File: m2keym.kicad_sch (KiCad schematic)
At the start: 0 parts

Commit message: [#56643] Create buses for interfaces, assign buses to blocks
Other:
- company: (none) -> Antmicro Ltd.
- title: (none) -> Com Express 7 baseboard
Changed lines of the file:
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@@
 (kicad_sch (version 20230121) (generator eeschema)
-  (paper "A4")
+  (paper "A3")
+  (title_block
+    (title "Com Express 7 baseboard")
+    (date "2024-03-22")
+    (rev "1.0.0")
+    (company "Antmicro Ltd.")
+  )
   (hierarchical_label "PCIe_x4{PCIe}" (shape input) (at 66.04 63.5 180) (fields_autoplaced)
     (effects (font (size 1.27 1.27)) (justify right))

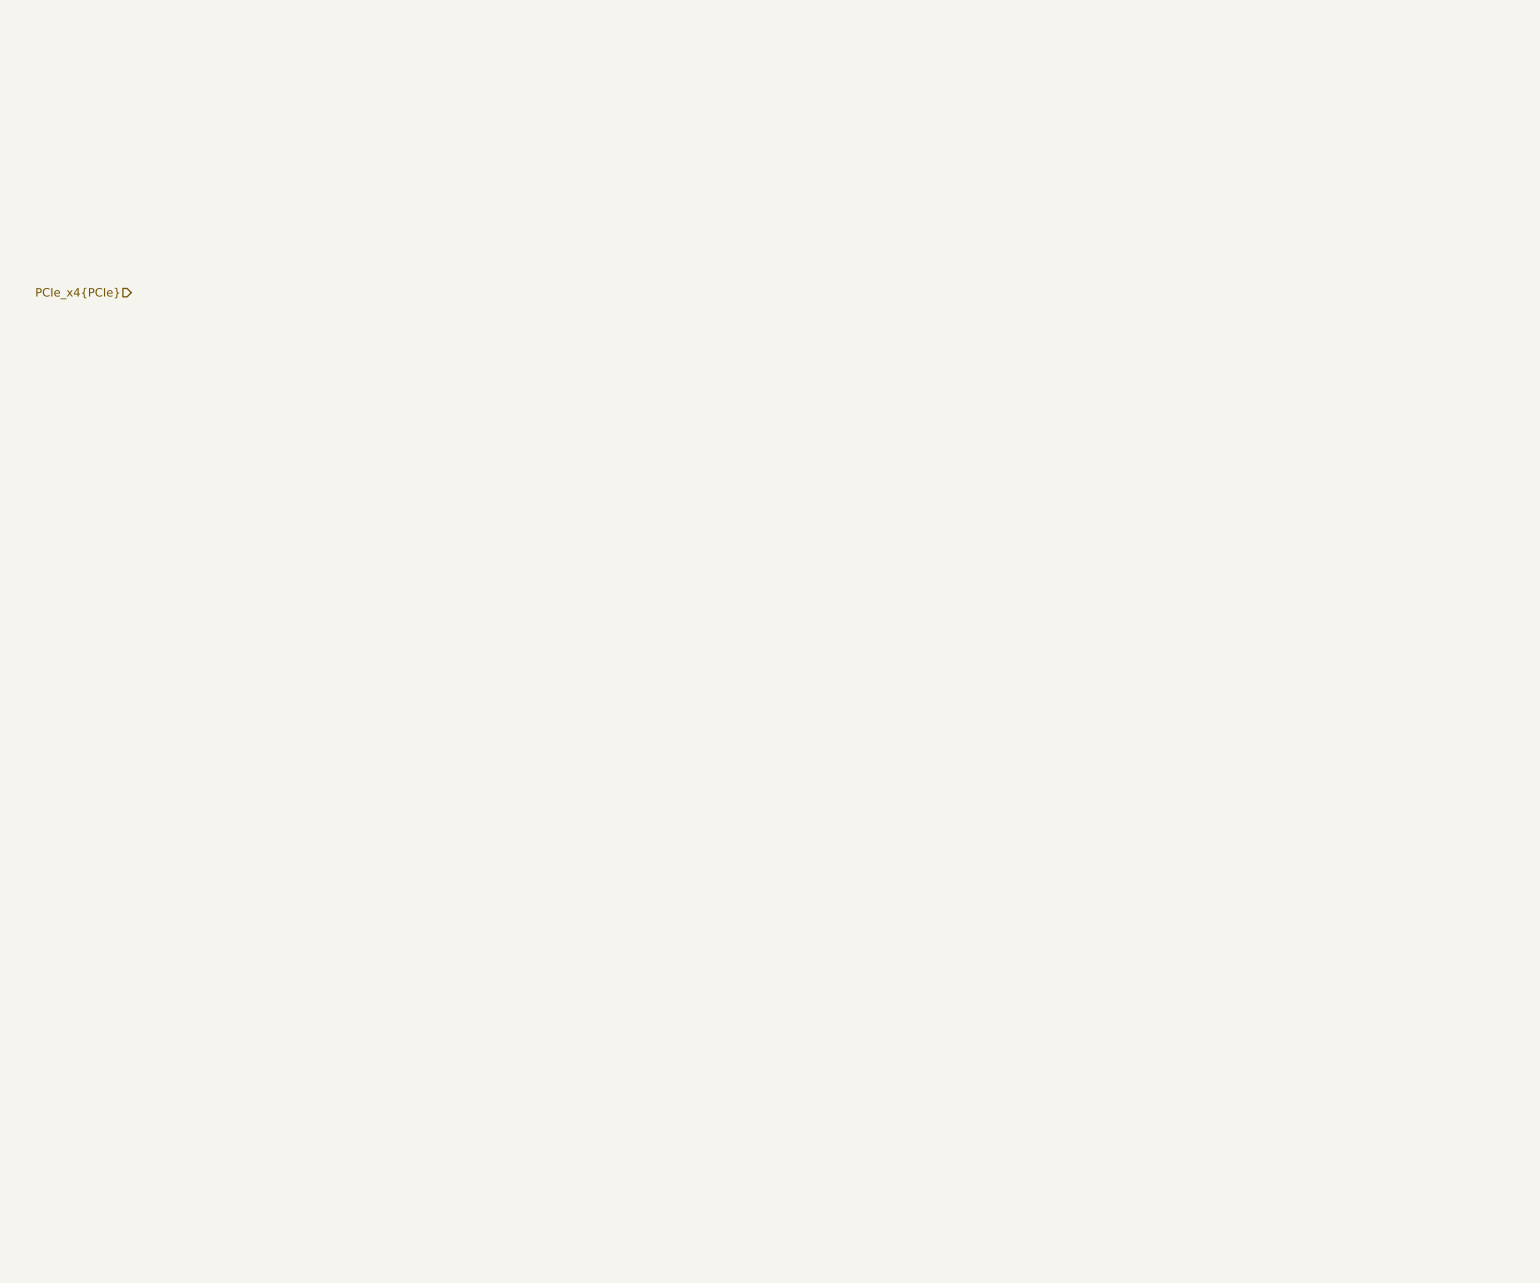
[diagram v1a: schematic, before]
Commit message: [#57056] Create schematics for M.2 and OCuLink connectors
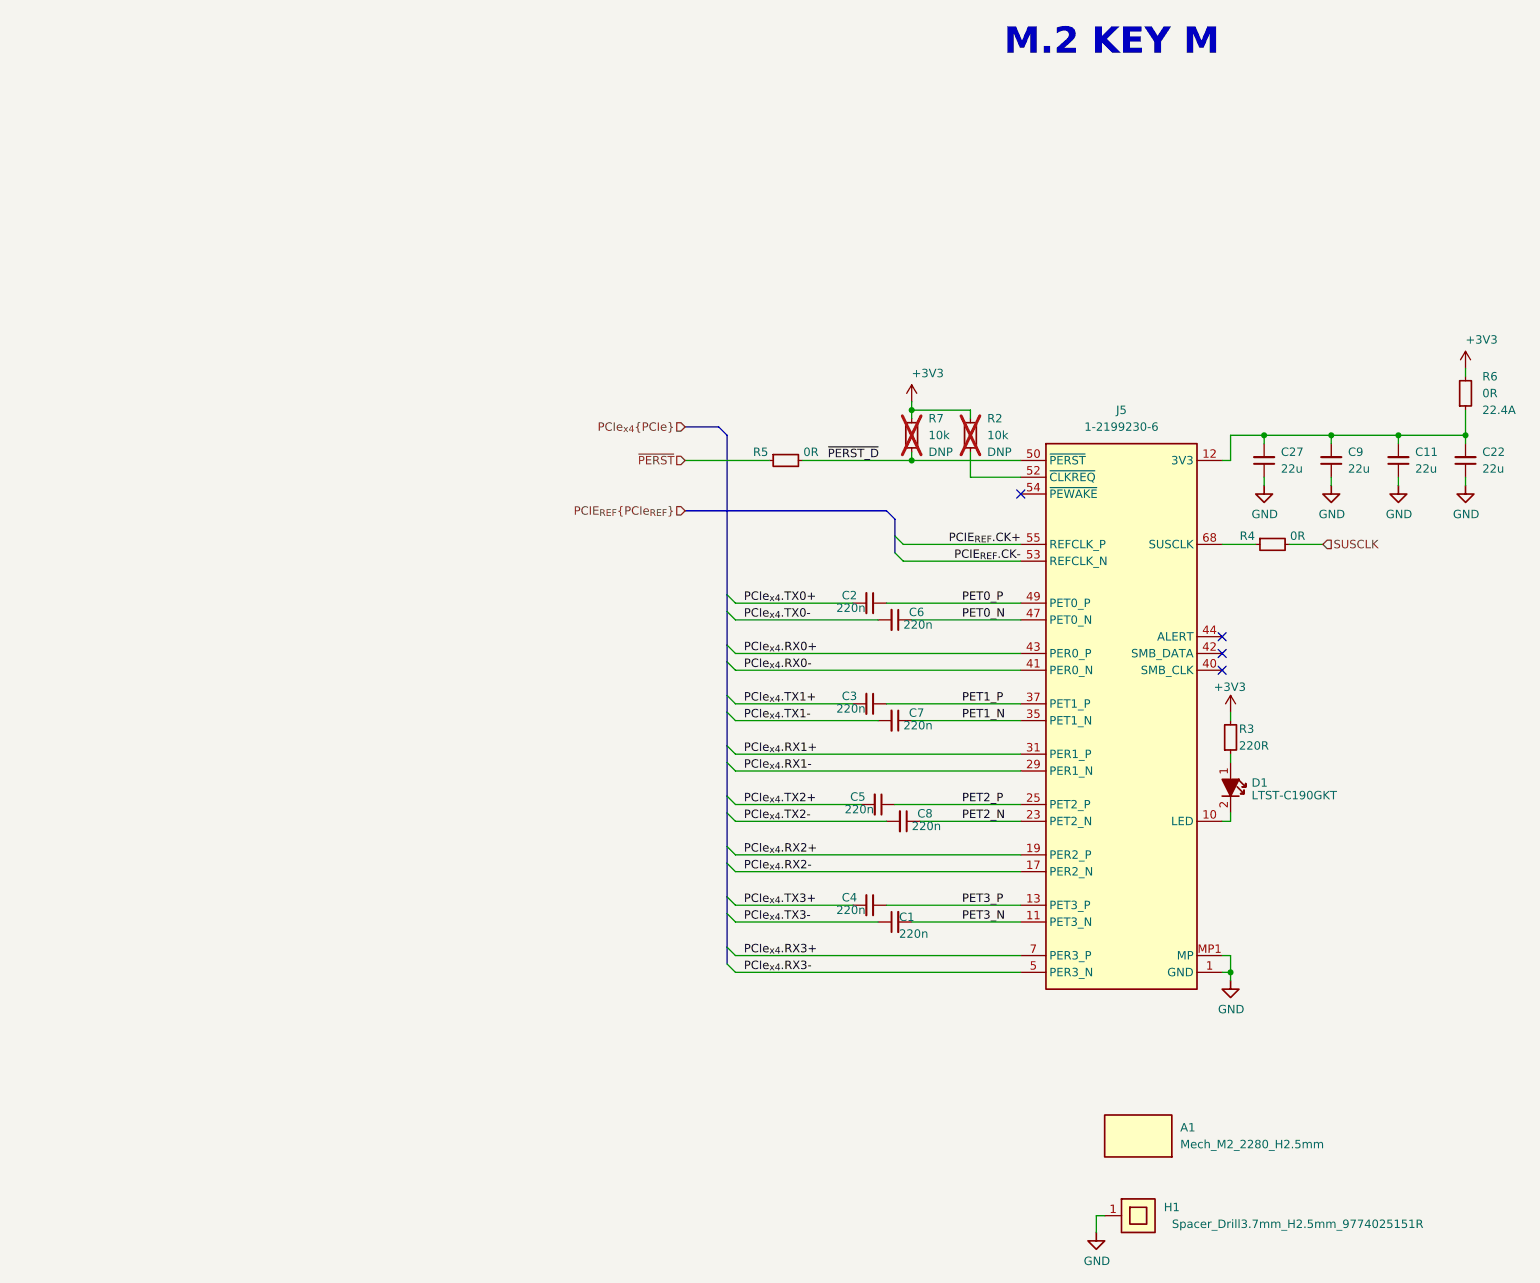
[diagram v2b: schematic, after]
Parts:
- added A1: Mech_M2_2280_H2.5mm, antmicro-footprints:Mech_M2_2280_H2.5mm, symbol antmicroModules:Mech_M2_2280_H2.5mm
- added C1, C2, C3, C4, C5, C6, C7, C8: C_220n_0402, antmicro-footprints:C_0402_1005Metric, symbol antmicroCapacitors0402:C_220n_0402
- added C11, C22, C27, C9: C_22u_0603, antmicro-footprints:C_0603_1608Metric, symbol antmicroCapacitors0603:C_22u_0603
- added D1: LED_G_0603_LTST-C190GKT, antmicro-footprints:LED_0603_1608Metric_G, symbol antmicroLEDIndicationDiscrete:LED_G_0603_LTST-C190GKT
- added H1: Spacer_Drill3.7mm_H2.5mm_9774025151R, antmicro-footprints:Spacer_Drill3.7mm_H2.5mm_9774025151R, symbol antmicroMechanicalParts:Spacer_Drill3.7mm_H2.5mm_9774025151R
- added J5: Bus_M.2_1-2199230-6, antmicro-footprints:Bus_M.2_Socket_Key_M_TE_1-2199230-6, symbol antmicroPciConnectors:Bus_M.2_1-2199230-6
- added R2, R7: R_10k_0402, antmicro-footprints:R_0402_1005Metric, symbol antmicroResistors0402:R_10k_0402
- added R3: R_220R_0402, antmicro-footprints:R_0402_1005Metric, symbol antmicroResistors0402:R_220R_0402
- added R4, R5: R_0R_0402, antmicro-footprints:R_0402_1005Metric, symbol antmicroResistors0402:R_0R_0402
- added R6: R_0R_22.4A_0603, antmicro-footprints:R_0603_1608Metric, symbol antmicroResistors0603:R_0R_22.4A_0603
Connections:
- new net: C11.2, C22.2, C27.2, C9.2, J5.12 (3V3), J5.14 (3V3), J5.16 (3V3), J5.18 (3V3), J5.2 (3V3), J5.4 (3V3), J5.70 (3V3), J5.72 (3V3), J5.74 (3V3), R6.1
- new net: J5.52 (~{CLKREQ}), R2.1
- new net: J5.68 (SUSCLK), R4.1
- new net: D1.1, R3.1
- new net: D1.2, J5.10 (LED)
- new net +3V3: R2.2, R3.2, R6.2, R7.2
- new net GND: C11.1, C22.1, C27.1, C9.1, H1.1, J5.1 (GND), J5.15 (GND), J5.21 (GND), J5.27 (GND), J5.3 (GND), J5.33 (GND), J5.39 (GND), J5.45 (GND), J5.51 (GND), J5.57 (GND), J5.71 (GND), J5.73 (GND), J5.75 (GND), J5.9 (GND), J5.MP1 (MP), J5.MP2 (MP)
- new net PCIE_{REF}.CK+: J5.55 (REFCLK_P)
- new net PCIE_{REF}.CK-: J5.53 (REFCLK_N)
- new net PCIe_{x4}.RX0+: J5.43 (PER0_P)
- new net PCIe_{x4}.RX0-: J5.41 (PER0_N)
- new net PCIe_{x4}.RX1+: J5.31 (PER1_P)
- new net PCIe_{x4}.RX1-: J5.29 (PER1_N)
- new net PCIe_{x4}.RX2+: J5.19 (PER2_P)
- new net PCIe_{x4}.RX2-: J5.17 (PER2_N)
- new net PCIe_{x4}.RX3+: J5.7 (PER3_P)
- new net PCIe_{x4}.RX3-: J5.5 (PER3_N)
- new net PCIe_{x4}.TX0+: C2.2
- new net PCIe_{x4}.TX0-: C6.2
- new net PCIe_{x4}.TX1+: C3.2
- new net PCIe_{x4}.TX1-: C7.2
- new net PCIe_{x4}.TX2+: C5.2
- new net PCIe_{x4}.TX2-: C8.2
- new net PCIe_{x4}.TX3+: C4.2
- new net PCIe_{x4}.TX3-: C1.1
- new net PET0_N: C6.1, J5.47 (PET0_N)
- new net PET0_P: C2.1, J5.49 (PET0_P)
- new net PET1_N: C7.1, J5.35 (PET1_N)
- new net PET1_P: C3.1, J5.37 (PET1_P)
- new net PET2_N: C8.1, J5.23 (PET2_N)
- new net PET2_P: C5.1, J5.25 (PET2_P)
- new net PET3_N: C1.2, J5.11 (PET3_N)
- new net PET3_P: C4.1, J5.13 (PET3_P)
- new net SUSCLK: R4.2
- new net ~{PERST_D}: J5.50 (~{PERST}), R5.2, R7.1
- new net ~{PERST}: R5.1
- no-connect marks 0 -> 4
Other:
- note added: "M.2 KEY M"

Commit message: [#57498] Add KR/SFP+
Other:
- note added: "TODO: CHECK IF AC COUPL CAPS NEEDED"
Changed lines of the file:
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@@
     (effects (font (size 4 4) (thickness 0.8) bold) (justify left bottom))
+  )
+  (text "TODO: CHECK IF AC COUPL CAPS NEEDED" (at 116.84 129.54 0)
+    (effects (font (size 1.27 1.27)) (justify left bottom))
   )
   (label "PCIe_{x4}.TX2-" (at 158.75 143.51 0) (fields_autoplaced)

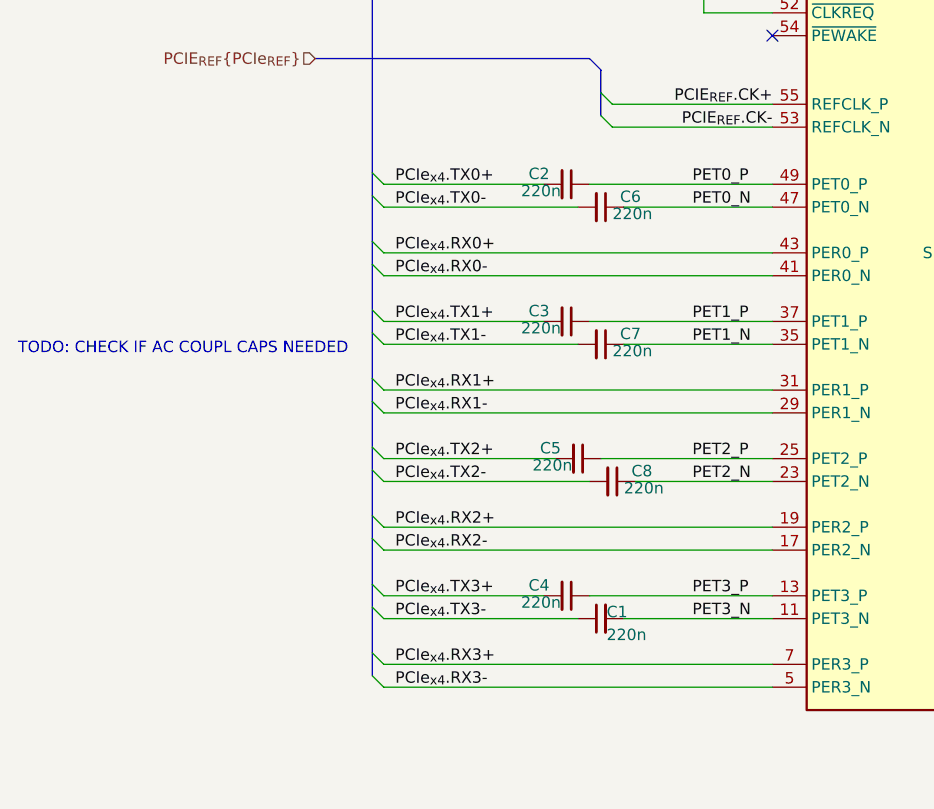
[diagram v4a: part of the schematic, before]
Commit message: [#57056] Remove AC coupling caps on PCIe lines
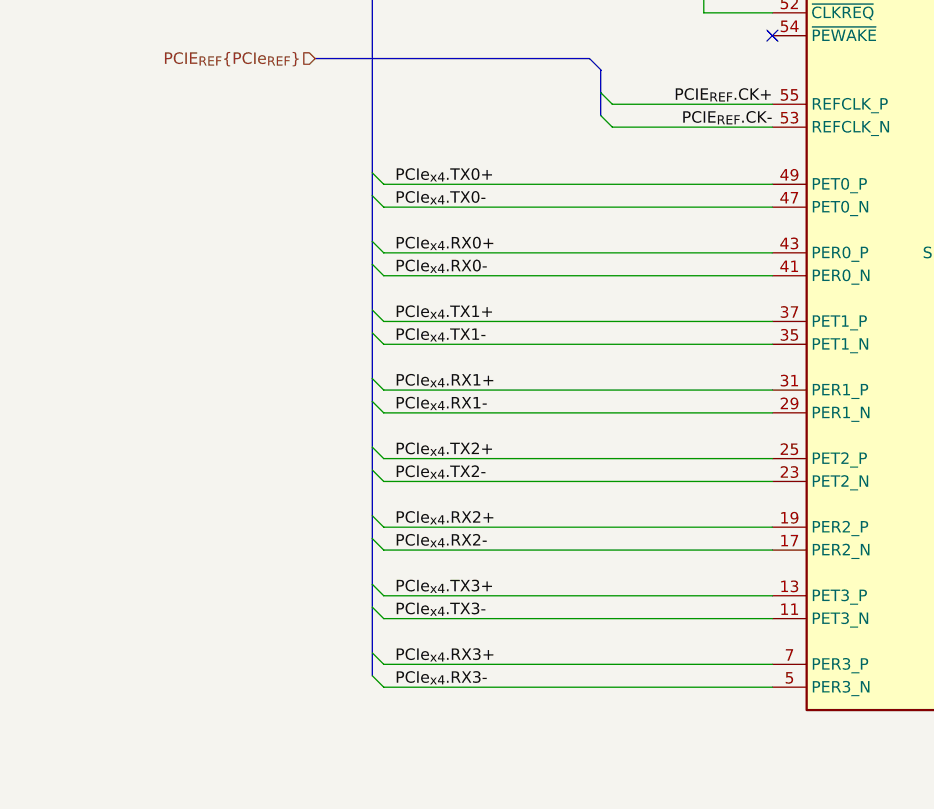
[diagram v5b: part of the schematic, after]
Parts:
- removed C1, C2, C3, C4, C5, C6, C7, C8: C_220n_0402, antmicro-footprints:C_0402_1005Metric, symbol antmicroCapacitors0402:C_220n_0402
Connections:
- net PET0_N is gone; now on net PCIe_{x4}.TX0-: J5.47 (PET0_N)
- net PET0_P is gone; now on net PCIe_{x4}.TX0+: J5.49 (PET0_P)
- net PET1_N is gone; now on net PCIe_{x4}.TX1-: J5.35 (PET1_N)
- net PET1_P is gone; now on net PCIe_{x4}.TX1+: J5.37 (PET1_P)
- net PET2_N is gone; now on net PCIe_{x4}.TX2-: J5.23 (PET2_N)
- net PET2_P is gone; now on net PCIe_{x4}.TX2+: J5.25 (PET2_P)
- net PET3_N is gone; now on net PCIe_{x4}.TX3-: J5.11 (PET3_N)
- net PET3_P is gone; now on net PCIe_{x4}.TX3+: J5.13 (PET3_P)
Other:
- note removed: "TODO: CHECK IF AC COUPL CAPS NEEDED"

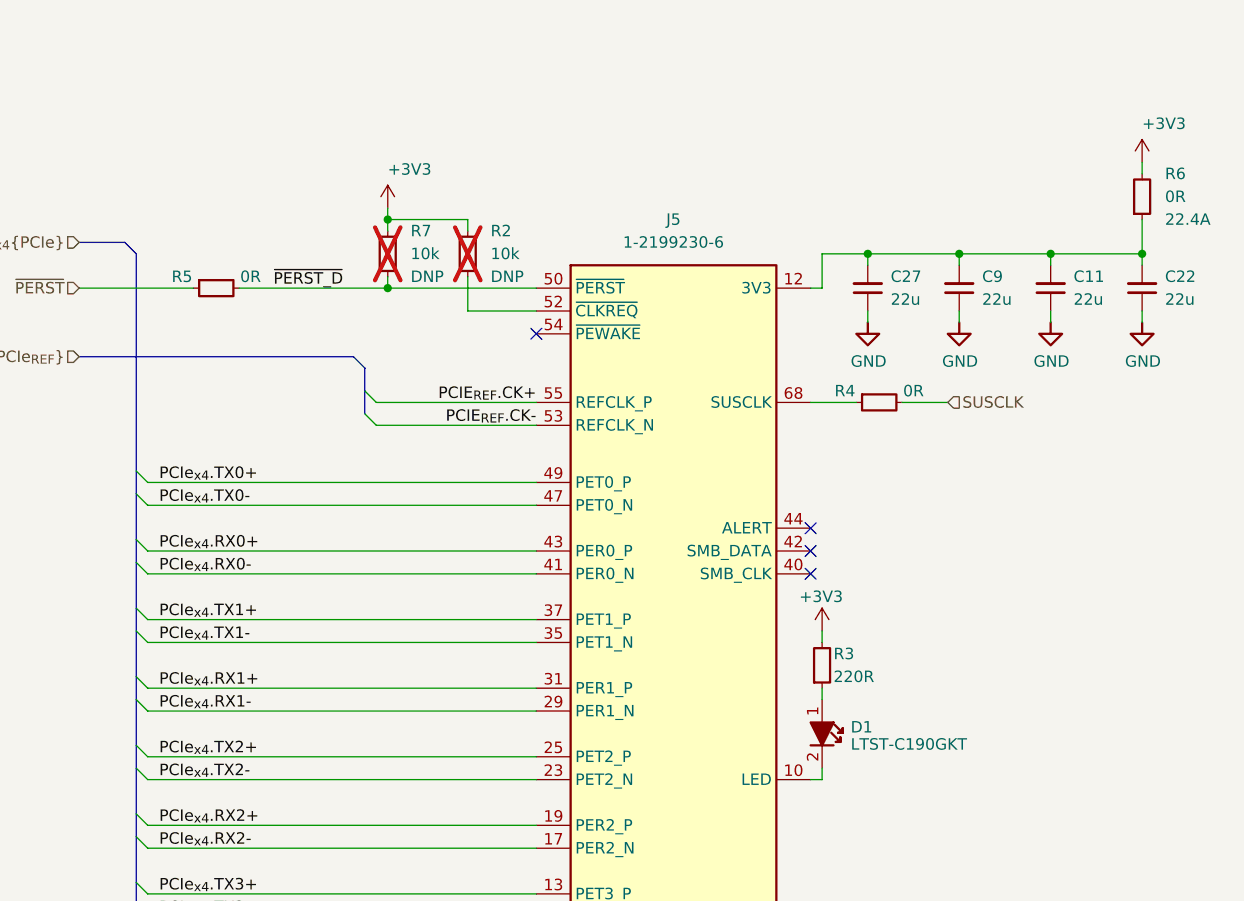
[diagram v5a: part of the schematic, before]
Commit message: [#58137] Update backplane connector pinout
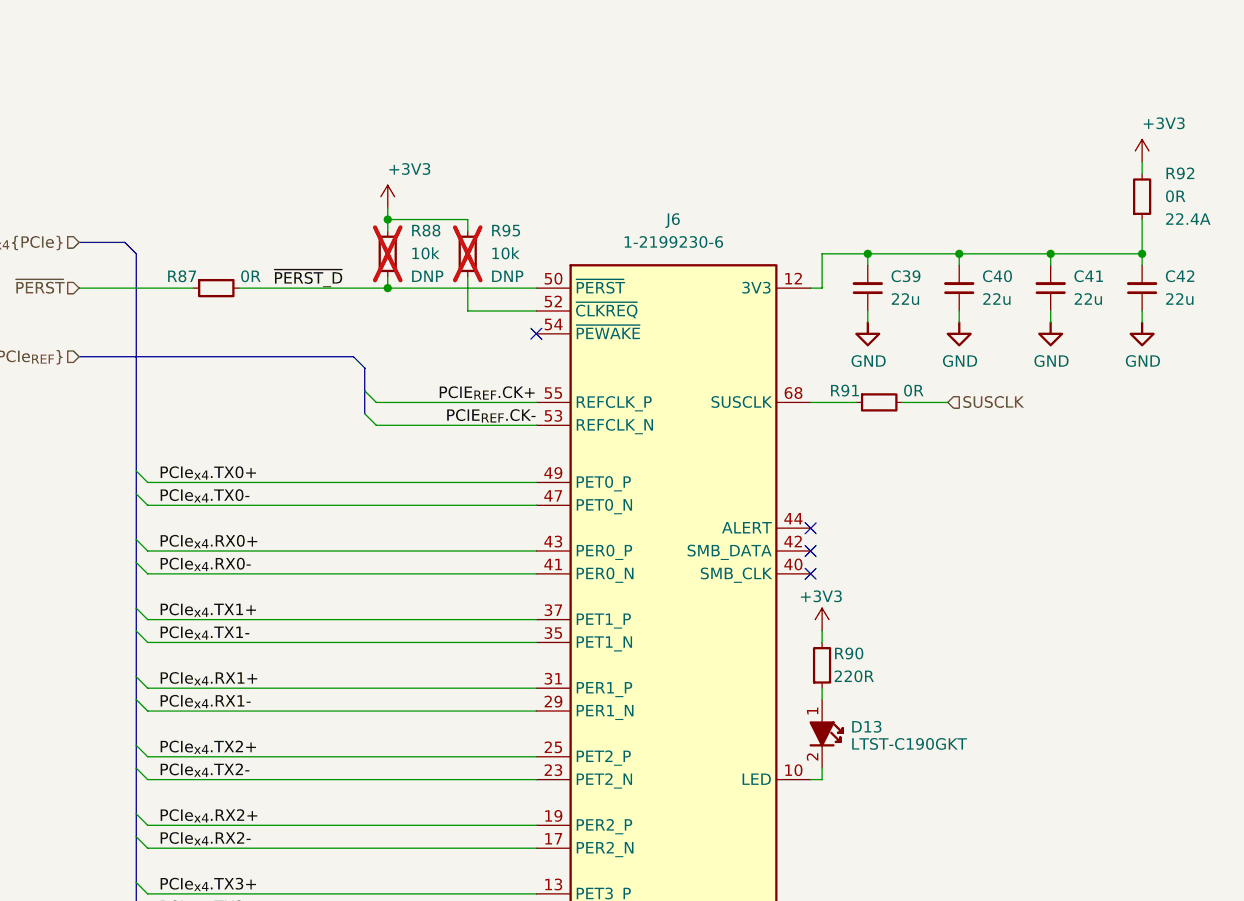
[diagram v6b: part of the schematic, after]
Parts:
- renumbered C27 to C39, C9 to C40, C11 to C41, C22 to C42, D1 to D13, J5 to J6, R5 to R87, R7 to R88, R3 to R90, R4 to R91, R6 to R92, R2 to R95
